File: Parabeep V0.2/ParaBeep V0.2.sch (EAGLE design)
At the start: 48 parts, among them J1 MICRO-SD_CARD_SOCKETPUSH-PUSH, Q1 500mA/300V, U1 ADXL345, U2 BQ25570RGRR, U3 TPS78330DDCRDDC5_TEX-L, U4 UBLOX_SAM_M8Q-0-10, U5 MS5803-14BA

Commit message: parabeep v0.2 ordered
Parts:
- removed J1: MICRO-SD_CARD_SOCKETPUSH-PUSH, SparkFun-Connectors:MICRO-SD_CARD_SOCKETPUSH-PUSH
- removed JP1: JUMPER-SMT_3_NO_SILK, SparkFun-Jumpers:JUMPER-SMT_3_NO_SILK
- removed U$5: ATSAMD51G19A, SparkFun-IC-Microcontroller:ATSAMD51G19A
- added C18: 0.1uF, SparkFun-Capacitors:0.1UF-0603-25V-(+80/-20%)
- added C19, C22: 33uF, SparkFun-Capacitors:CAP-1206
- added C20, C21: 6pF, SparkFun-Capacitors:6PF-0402-50V-0.5%
- added D2: GREEN, SparkFun-LED:LED-GREEN0603
- added IC2: MCP73811/2, adafruit:MCP73811/2
- added J2: (no value), SparkFun-Connectors:USB_MICRO-B_FEMALE-SMT
- added R11, R12, R25, R8: (no value), SparkFun-Resistors:RESISTOR0402
- added U$2: DMG1013UW-7, DMG1013UW-7:DMG1013UW-7
- added U6: ATSAMD51J20A-A, SparkFun-IC-Microcontroller:ATSAMD51J20A-A
- added U7: AT25SF128A-SHB-T, AT25SF128A-SHB-T:AT25SF128A-SHB-T
- added Y1: 32.768kHz, SparkFun-Clocks:CRYSTAL-32.768KHZSMD-3.2X1.5
- C1: value 4.7uF -> 33uF; device SparkFun-Capacitors:4.7UF-0603-6.3V-(10%) -> SparkFun-Capacitors:CAP-1206
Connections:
- removed net SC_MEM: J1.CS
- removed net SPI_MISO: J1.DO, U1.SDO, U5.SDO
- removed net SPI_MOSI: J1.DI, U1.SDA, U5.SDA/SDI
- removed net SPI_SCK: J1.SCK, U1.SCL, U5.SCL/SCLK
- removed net USART_RX: U4.TX
- removed net USART_TX: U4.RX
- new net CS_MEM: R11.1, U6.PB00, U7.!CS
- new net D+: J2.D+, U6.PA25
- new net D-: J2.D-, U6.PA24
- new net LED: R12.2, U6.PB16
- new net N$14: C18.2, U7.VCC
- new net N$17: D2.A, R12.1
- new net N$18: IC2.PROG, R25.2
- new net RSTLCK: U$2.G, U6.PB22
- new net SERCOM0_MISO: U1.SDO, U5.SDO, U6.PA10
- new net SERCOM0_MOSI: U1.SDA, U5.SDA/SDI, U6.PA08
- new net SERCOM0_SCK: U1.SCL, U5.SCL/SCLK, U6.PA09
- new net SERCOM5_MISO: U6.PB01, U7.SO(I/O1)
- new net SERCOM5_MOSI: U6.PB02, U7.SI(I/O0)
- new net SERCOM5_SCK: U6.PB03, U7.SCK
- new net SERCOM7_RX: U4.TX, U6.PB31
- new net SERCOM7_TX: U4.RX, U6.PB30
- new net VBUS: IC2.CE, IC2.VDD, J2.VBUS
- net !RESET: now also R5.2, U$2.D
- net BUTTON: now also U$2.S, U$3.2; no longer R5.2, U$3.1
- net BUZZER: now also U6.PA20
- net CS_ACCEL: now also R8.1, U6.PA11
- net CS_BARO: now also U6.PA07
- net GND: now also C19.2, C20.1, C21.1, C22.2, D2.C, IC2.VSS, R25.1, SOL-1.S, U6.GND, U7.GND; no longer SOL-2.S, U$5.GND@18, U$5.GND@35, U$5.GND@42, U$5.GND@5
- net GPS_INT: now also U6.PA03
- net N$1: now also C20.2, U6.PA00, Y1.2; no longer C3.1
- net N$11: now also SOL-2.S; no longer SOL-1.S
- net N$19: now also U6.VDDCORE; no longer U$5.VDDCORE
- net N$2: now also C21.2, U6.PA01, Y1.1; no longer D1.C, JP1.2, SG1.2
- net N$23: now also C3.1, U6.VDDANA; no longer U$5.VDDANA
- net RX: now also U6.PA23
- net SWCLK: now also U6.PA30
- net SWDIO: now also U6.PA31
- net TX: now also U6.PA22
- net VCC-ISO: now also C19.1, U6.VDDIO; no longer C1.1, U$5.VDDIO@17, U$5.VDDIO@36, U$5.VDDIO@44
- net VCC_1: now also C1.1, C18.1, C22.1, D1.C, R11.2, R8.2, SG1.2, U$3.1, U7.!HOLD!/!RESET!(I/O3), U7.!WP!(I/O2); no longer JP1.3, U$3.2
- net VIN: now also IC2.VBAT; no longer JP1.1
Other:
- moved on the sheet: C1, C11, C12, C14, C15, C16, C3, C9, D1, L2, Q1, R13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

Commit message: parabeep v0.2 order third try
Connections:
- new net EN: U3.EN, U6.PB12
- net VCC-ISO: now also U$3.1
- net VCC_1: no longer U$3.1
- net VIN: no longer U3.EN
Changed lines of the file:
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@@
 <part name="C12" library="SparkFun-Capacitors" deviceset="0.1UF" device="-0603-25V-(+80/-20%)" value="10uF"/>
 <part name="L2" library="SparkFun-Coils" deviceset="INDUCTOR" device="FB-30OHM"/>
-<part name="SUPPLY9" library="SparkFun-PowerSymbols" deviceset="VCC_1" device=""/>
 <part name="R5" library="SparkFun-Resistors" deviceset="RESISTOR" device="0402" value=" "/>
 <part name="GND4" library="SparkFun-Aesthetics" deviceset="GND" device=""/>
@@
 <part name="R12" library="SparkFun-Resistors" deviceset="RESISTOR" device="0402" value=" "/>
 <part name="GND23" library="SparkFun-Aesthetics" deviceset="GND" device=""/>
+<part name="U$6" library="SparkFun-PowerSymbols" deviceset="VCC-ISO" device=""/>
 </parts>
 <sheets>
@@
 <attribute name="VALUE" x="58.42" y="184.15" size="1.778" layer="96" font="vector" rot="R90" align="top-left"/>
 </instance>
-<instance part="SUPPLY9" gate="G$2" x="236.22" y="38.1" smashed="yes">
-<attribute name="VALUE" x="241.3" y="40.894" size="1.778" layer="96" align="bottom-center"/>
-</instance>
 <instance part="R5" gate="G$1" x="269.24" y="15.24" smashed="yes" rot="R90">
 <attribute name="NAME" x="267.7414" y="11.43" size="1.27" layer="95" rot="R90"/>
@@
 <instance part="GND23" gate="1" x="190.5" y="22.86" smashed="yes">
 <attribute name="VALUE" x="193.04" y="22.86" size="1.778" layer="96"/>
+</instance>
+<instance part="U$6" gate="G$1" x="236.22" y="38.1" smashed="yes">
+<attribute name="VALUE" x="234.696" y="46.736" size="1.778" layer="96" rot="R270" align="bottom-center"/>
 </instance>
 </instances>
@@
 <wire x1="378.46" y1="121.92" x2="378.46" y2="124.46" width="0.1524" layer="91"/>
 </segment>
-<segment>
-<pinref part="U$3" gate="G$1" pin="1"/>
-<wire x1="246.38" y1="33.02" x2="236.22" y2="33.02" width="0.1524" layer="91"/>
-<pinref part="SUPPLY9" gate="G$2" pin="VCC_1"/>
-<wire x1="236.22" y1="33.02" x2="236.22" y2="38.1" width="0.1524" layer="91"/>
-</segment>
 </net>
 <net name="VIN" class="0">
@@
 <pinref part="U3" gate="A" pin="IN"/>
 <wire x1="27.94" y1="254" x2="25.4" y2="254" width="0.1524" layer="91"/>
-<pinref part="U3" gate="A" pin="EN"/>
-<wire x1="27.94" y1="251.46" x2="25.4" y2="251.46" width="0.1524" layer="91"/>
-<wire x1="25.4" y1="254" x2="25.4" y2="251.46" width="0.1524" layer="91"/>
 <wire x1="15.24" y1="254" x2="15.24" y2="251.46" width="0.1524" layer="91"/>
 <junction x="25.4" y="254"/>
@@
 <pinref part="U$4" gate="G$1" pin="VCC-ISO"/>
 </segment>
+<segment>
+<pinref part="U$3" gate="G$1" pin="1"/>
+<wire x1="246.38" y1="33.02" x2="236.22" y2="33.02" width="0.1524" layer="91"/>
+<wire x1="236.22" y1="33.02" x2="236.22" y2="38.1" width="0.1524" layer="91"/>
+<pinref part="U$6" gate="G$1" pin="VCC-ISO"/>
+</segment>
 </net>
 <net name="N$19" class="0">
@@
 </segment>
 </net>
+<net name="EN" class="0">
+<segment>
+<pinref part="U6" gate="G$1" pin="PB12"/>
+<wire x1="195.58" y1="134.62" x2="198.12" y2="134.62" width="0.1524" layer="91"/>
+<label x="198.12" y="134.62" size="1.778" layer="95"/>
+</segment>
+<segment>
+<pinref part="U3" gate="A" pin="EN"/>
+<wire x1="27.94" y1="251.46" x2="25.4" y2="251.46" width="0.1524" layer="91"/>
+<label x="25.4" y="251.46" size="1.778" layer="95" rot="R180"/>
+</segment>
+</net>

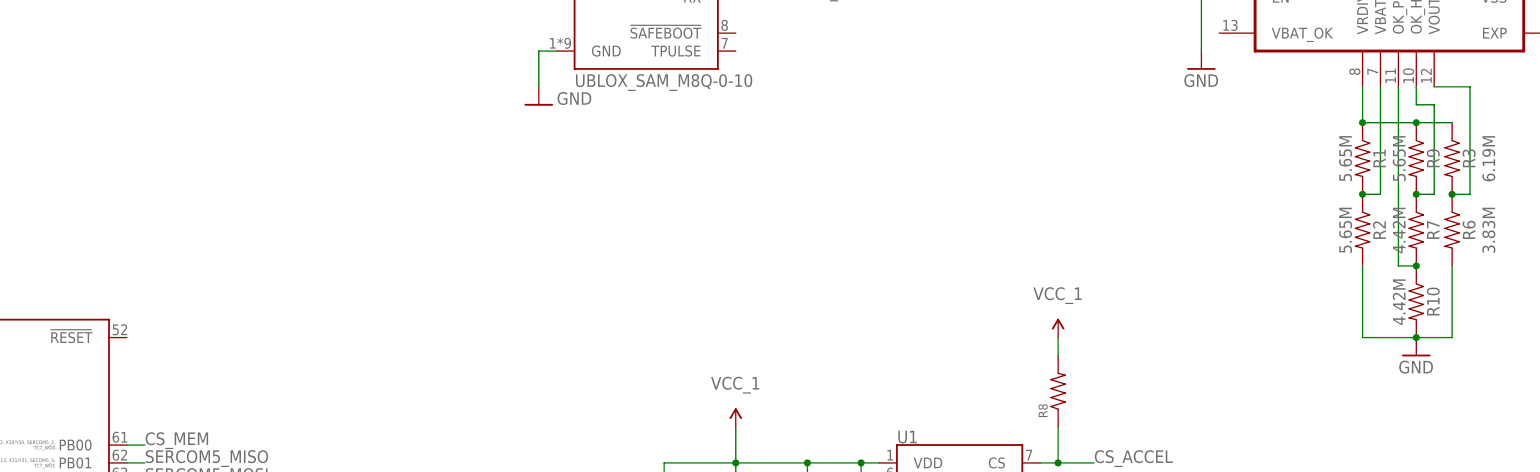
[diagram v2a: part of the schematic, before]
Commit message: working on parabeep v0.2, accel not working yet
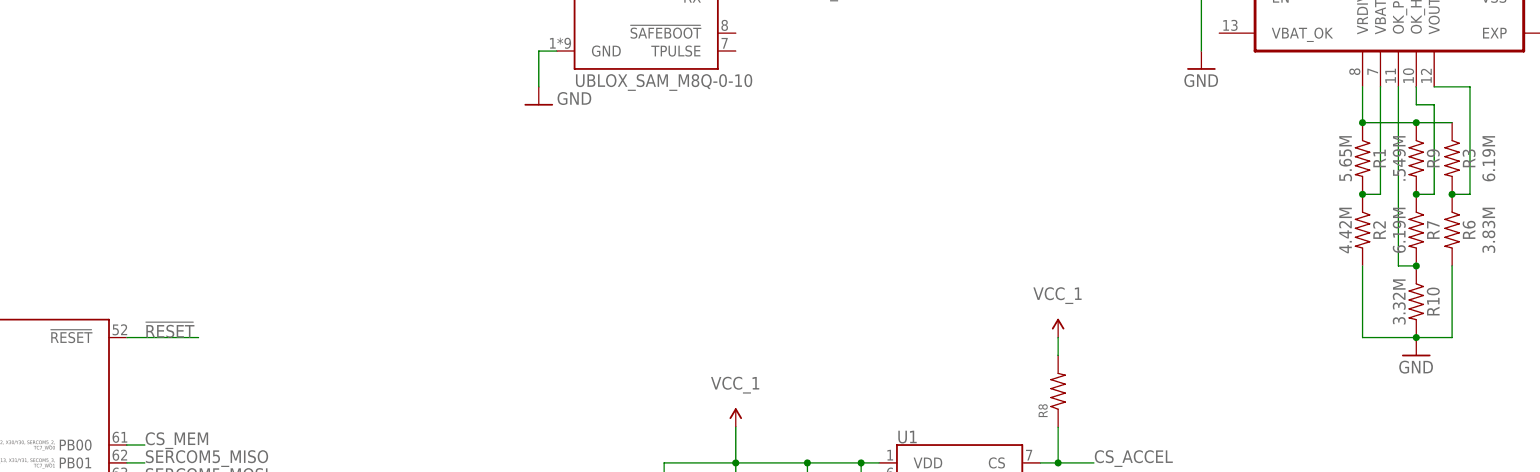
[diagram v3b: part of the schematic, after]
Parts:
- R10: value 4.42M -> 3.32M
- R2: value 5.65M -> 4.42M
- R7: value 4.42M -> 6.19M
- R9: value 5.65M -> .549M
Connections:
- net !RESET: now also U6.!RESET
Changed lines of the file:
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@@
 <part name="R3" library="SparkFun-Resistors" deviceset="RESISTOR" device="0603" value="6.19M"/>
 <part name="R6" library="SparkFun-Resistors" deviceset="RESISTOR" device="0603" value="3.83M"/>
-<part name="R7" library="SparkFun-Resistors" deviceset="RESISTOR" device="0603" value="4.42M"/>
-<part name="R9" library="SparkFun-Resistors" deviceset="RESISTOR" device="0603" value="5.65M"/>
+<part name="R7" library="SparkFun-Resistors" deviceset="RESISTOR" device="0603" value="6.19M"/>
+<part name="R9" library="SparkFun-Resistors" deviceset="RESISTOR" device="0603" value=".549M"/>
 <part name="L1" library="SparkFun-Coils" deviceset="INDUCTOR" device="-CDRH-4.7UH" value="22µH - 744031220"/>
 <part name="GND5" library="SparkFun-Aesthetics" deviceset="GND" device=""/>
@@
 <part name="C8" library="SparkFun-Capacitors" deviceset="4.7UF" device="-0603-6.3V-(10%)" value="4.7uF"/>
 <part name="R1" library="SparkFun-Resistors" deviceset="RESISTOR" device="0603" value="5.65M"/>
-<part name="R2" library="SparkFun-Resistors" deviceset="RESISTOR" device="0603" value="5.65M"/>
-<part name="R10" library="SparkFun-Resistors" deviceset="RESISTOR" device="0603" value="4.42M"/>
+<part name="R2" library="SparkFun-Resistors" deviceset="RESISTOR" device="0603" value="4.42M"/>
+<part name="R10" library="SparkFun-Resistors" deviceset="RESISTOR" device="0603" value="3.32M"/>
 <part name="GND1" library="SparkFun-Aesthetics" deviceset="GND" device=""/>
 <part name="GND10" library="SparkFun-Aesthetics" deviceset="GND" device=""/>
@@
 <junction x="269.24" y="20.32"/>
 </segment>
+<segment>
+<pinref part="U6" gate="G$1" pin="!RESET"/>
+<wire x1="195.58" y1="182.88" x2="205.74" y2="182.88" width="0.1524" layer="91"/>
+<label x="198.12" y="182.88" size="1.778" layer="95"/>
+</segment>
 </net>
